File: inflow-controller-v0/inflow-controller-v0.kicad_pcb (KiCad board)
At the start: 2 copper layers, 16 parts, among them CN401 Conn_02x04_Odd_Even, J101 Conn_01x02, J201 Conn_01x02, J301 Conn_01x06, J401 Conn_01x02, J402 Conn_01x02, J403 Conn_01x06, SW101 SW_Push, SW201 SW_Push, SW301 SW_Push

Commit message: Modify analog stick footprint (dimensions seemed to be wrong), route most of the PCBs
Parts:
- removed H301, H302, H303, H304: MountingHole_Pad, TestPoint:TestPoint_Loop_D2.54mm_Drill1.5mm_Beaded
- removed RV301, RV302: R_POT, Connector_PinHeader_2.54mm:PinHeader_1x03_P2.54mm_Vertical
- removed SW301: SW_Push, Button_Switch_THT:SW_PUSH_6mm
- added X301: XB1_STICK, xb1-stick:xb1-stick, F.Cu at (110.6, 127.2)
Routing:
- net /AVDD3: track 0.00 -> 29.5 mm
- net /X3: track 0.00 -> 23.4 mm
- net /Y3: track 0.00 -> 21.3 mm, vias 0 -> 1
- net /DGND3: track 0.00 -> 19.7 mm
- net /BTN3: track 0.00 -> 19.3 mm
- net /BTN1_4: track 0.00 -> 18.1 mm
- net /DGND1_4: track 0.00 -> 17.0 mm
- net /BTN2_4: track 0.00 -> 12.8 mm, vias 0 -> 1
- net /X3_4: track 0.00 -> 9.12 mm
- net /AGND3: track 0.00 -> 8.90 mm
- net /AVDD3_4: track 0.00 -> 8.67 mm
- net /BTN3_4: track 0.00 -> 8.59 mm
- net /Y3_4: track 0.00 -> 6.13 mm
- net /AGND3_4: track 0.00 -> 5.79 mm
- added copper zone on F.Cu, net /AGND3

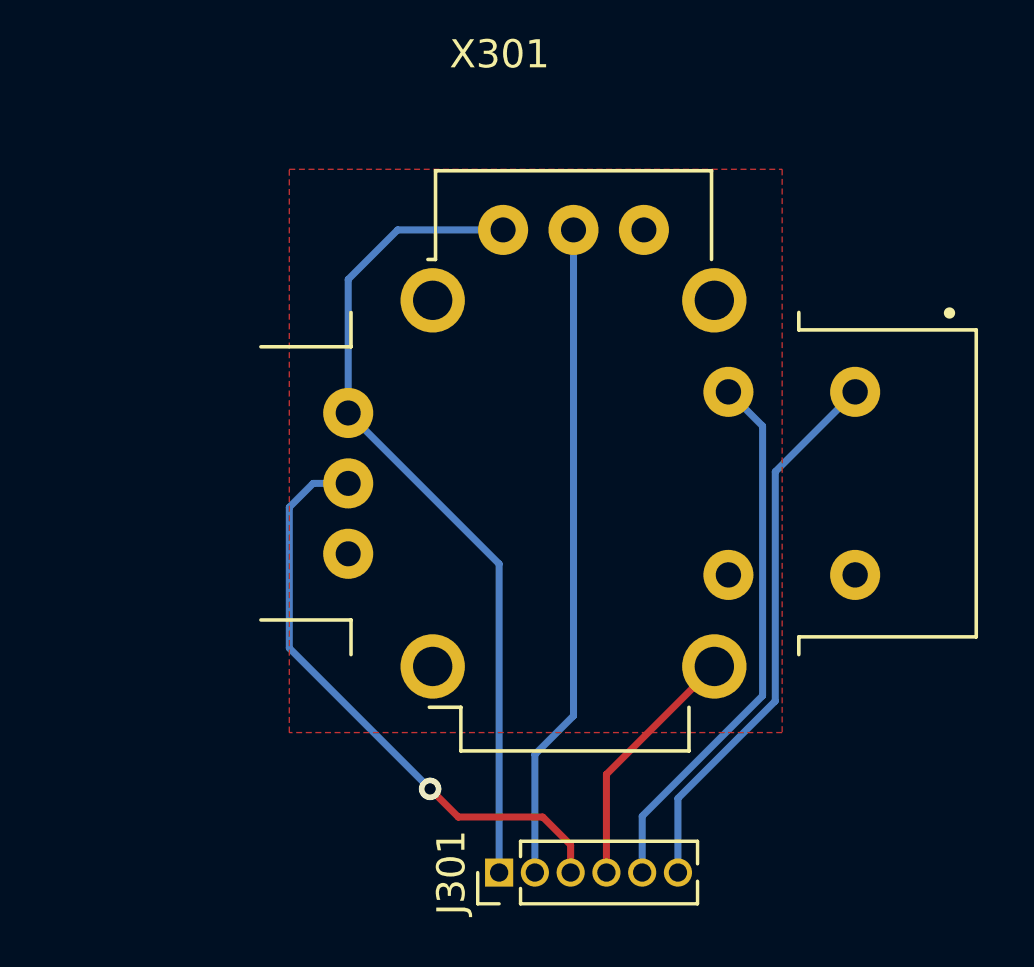
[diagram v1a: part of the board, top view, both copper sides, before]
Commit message: Update xb1-stick joystick footprint and symbol
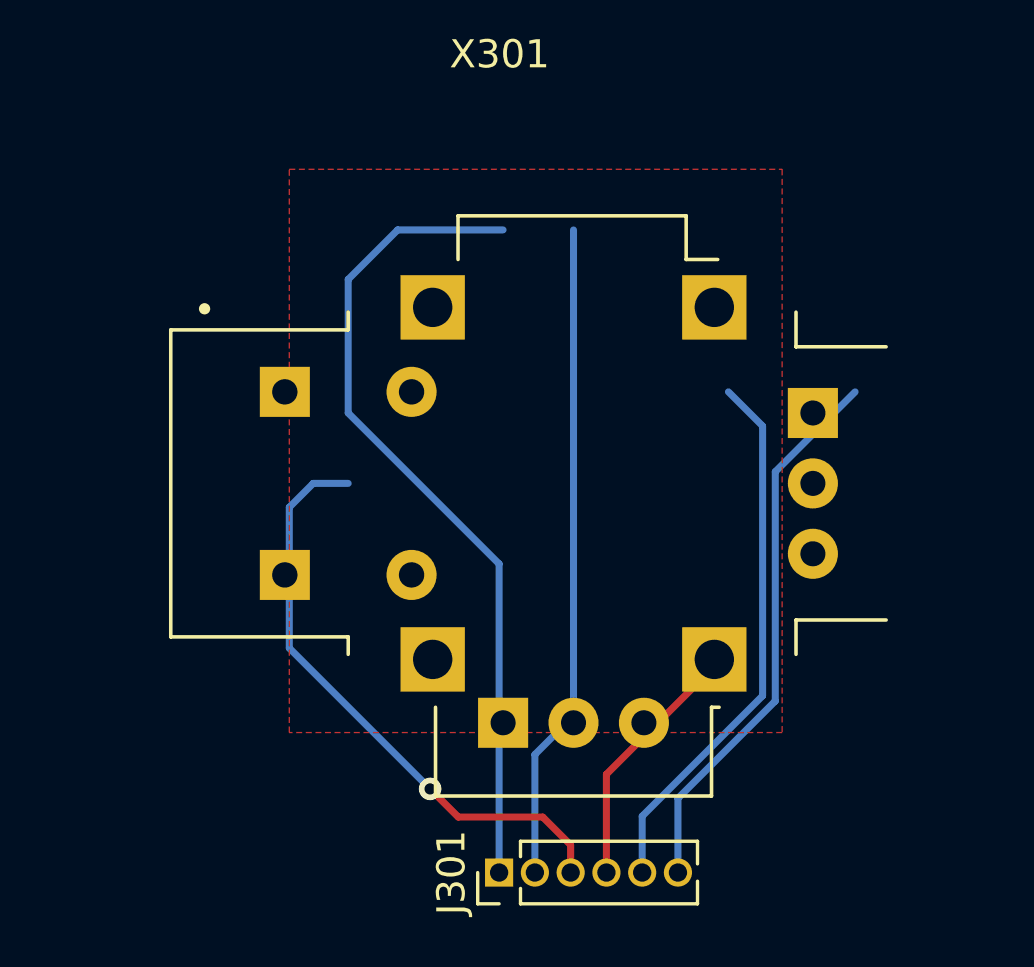
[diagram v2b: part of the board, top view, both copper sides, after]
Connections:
- X301 pad B1A: /BTN3 -> /DGND3
- X301 pad B1B: (no net) -> /DGND3
- X301 pad B2A: /DGND3 -> /BTN3
- X301 pad B2B: (no net) -> /BTN3
- X301 pad H1: /AVDD3 -> /AGND3
- X301 pad H3: /AGND3 -> /AVDD3
- X301 pad V1: /AVDD3 -> /AGND3
- X301 pad V3: /AGND3 -> /AVDD3

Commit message: v0 out for production
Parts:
- J101: moved to B.Cu
- J202: renamed from J201; moved to B.Cu
- J303: renamed from J301; moved to B.Cu
- moved J402 34.9 mm to (116.2, 110.4), turned to 270 degrees
- moved J401 33.1 mm to (121.3, 110.4), turned to 270 degrees
- moved J403 26.0 mm to (121.3, 105.3), turned to 270 degrees
- moved CN401 24.1 mm to (113.7, 100.2), turned to 90 degrees
- moved SW101 24.0 mm to (102.5, 96.5), turned to 0 degrees
- moved SW201 22.6 mm to (102.5, 108.5)
- moved J101 22.1 mm to (98.5, 97.2)
- moved J202 19.5 mm to (98.5, 109.2), turned to 0 degrees
- moved J303 7.33 mm to (104.5, 134.5)
- moved X301 2.23 mm to (110.0, 125.0)
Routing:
- net /X3: track 23.4 -> 8.46 mm
- net /DGND2: track 0.00 -> 10.1 mm
- net /AVDD3: track 29.5 -> 19.8 mm
- net /DGND1: track 0.00 -> 9.69 mm
- net /BTN2: track 0.00 -> 9.46 mm
- net /BTN1: track 0.00 -> 9.46 mm
- net /AGND3: track 8.90 -> 0.00 mm
- net /DGND3: track 19.7 -> 13.4 mm
- net /Y3: track 21.3 -> 27.4 mm, vias 1 -> 0
- net /BTN3: track 19.3 -> 14.8 mm
- added copper zone on B.Cu, net (none)
- added copper zone on F.Cu, net (none)
- added copper zone on B.Cu, net /AGND3
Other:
- board outline added: 29 x 46 mm
